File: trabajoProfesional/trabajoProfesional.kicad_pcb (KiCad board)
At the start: 2 copper layers, 21 parts, among them J1 SYSOUT, J2 BATPositve, J3 BATNegative, J4 GPIO5, J5 GPIO4, J6 GPIO3, J7 GPIO2, J8 GPIO1, U1 TS51224-M000WCSR

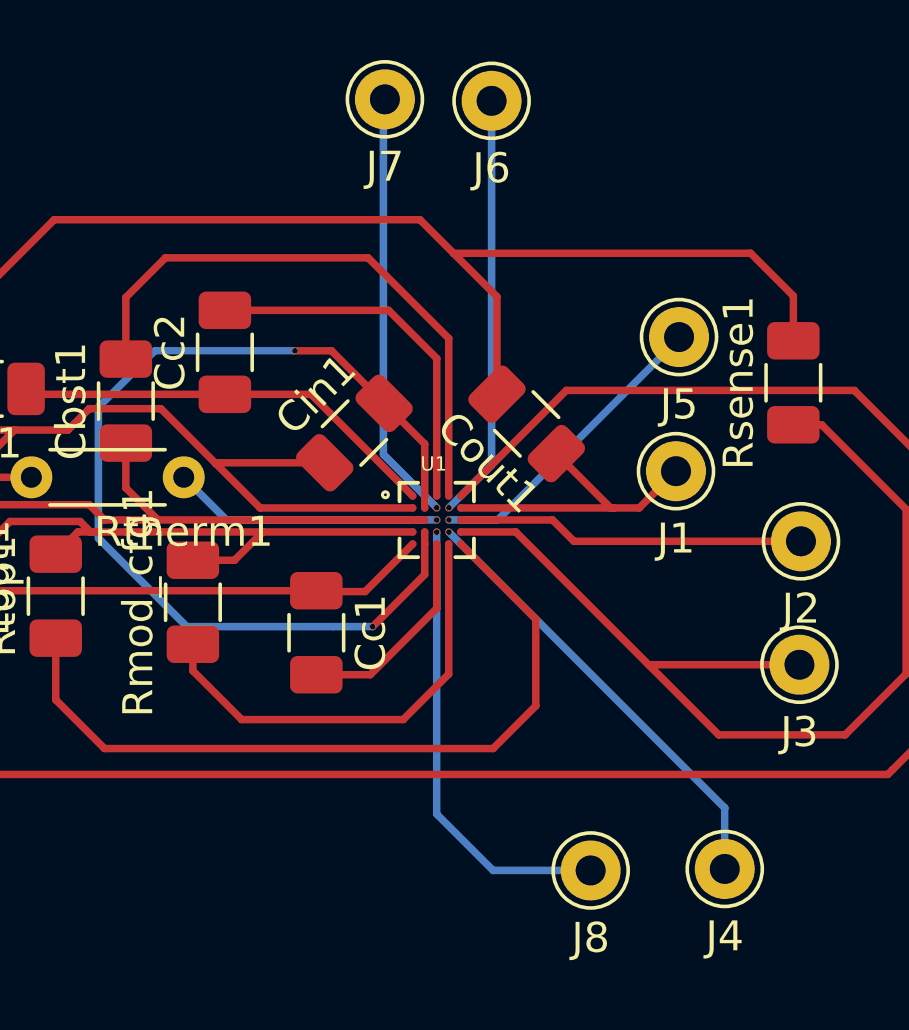
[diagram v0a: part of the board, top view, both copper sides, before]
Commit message: ahora se modifico la via para que quede lo mas grande posible y fuera del pin VGA
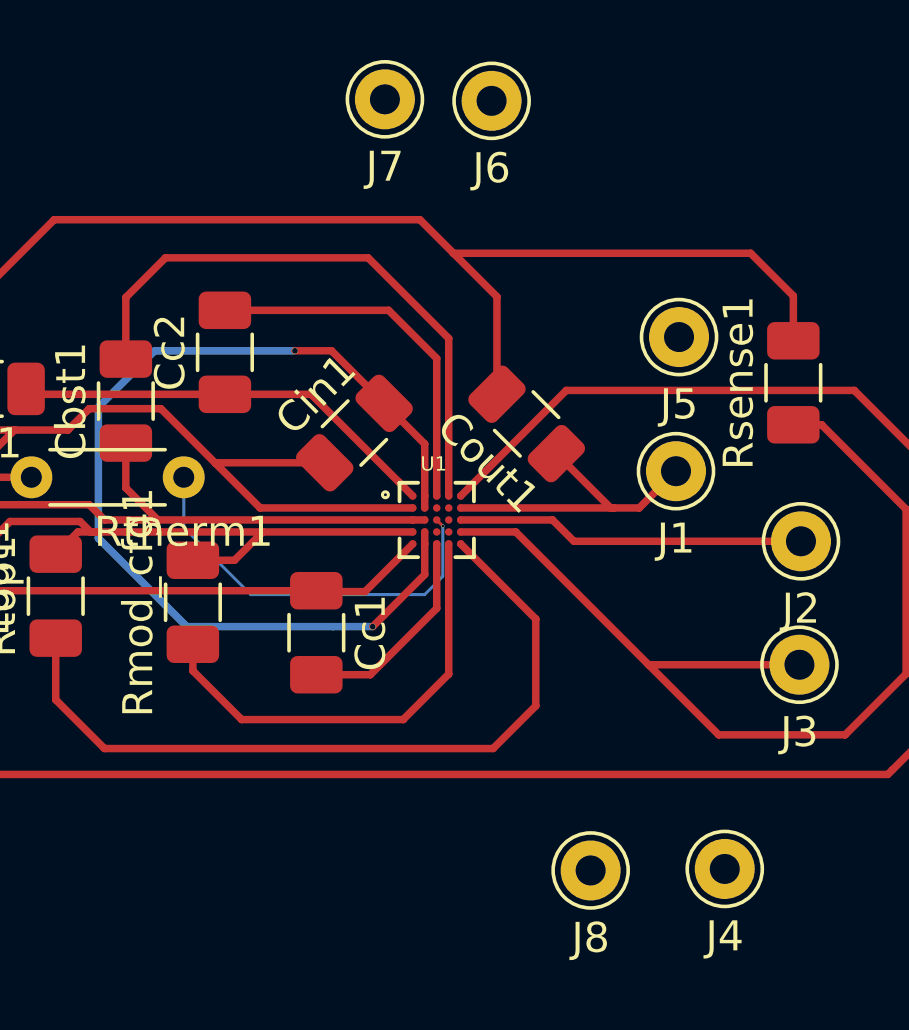
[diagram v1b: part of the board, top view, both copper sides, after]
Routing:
- net Net-(J8-Pad1): track 15.3 -> 0.00 mm, vias 1 -> 0
- net Net-(J4-Pad1): track 15.0 -> 0.00 mm, vias 1 -> 0
- net Net-(J7-Pad1): track 14.4 -> 0.00 mm, vias 1 -> 0
- net Net-(J6-Pad1): track 14.2 -> 0.00 mm, vias 1 -> 0
- net Net-(J5-Pad1): track 10.2 -> 0.00 mm, vias 1 -> 0
- net Net-(Rtherm1-Pad1): track 9.02 -> 13.5 mm

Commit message: va el parche con el ultimo mod del los pines anulados
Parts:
- removed J4: GPIO5, Connector_Pin:Pin_D1.0mm_L10.0mm
- removed J5: GPIO4, Connector_Pin:Pin_D1.0mm_L10.0mm
- removed J6: GPIO3, Connector_Pin:Pin_D1.0mm_L10.0mm
- removed J7: GPIO2, Connector_Pin:Pin_D1.0mm_L10.0mm
- removed J8: GPIO1, Connector_Pin:Pin_D1.0mm_L10.0mm
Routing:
- net Net-(Cin1-Pad2): track 33.7 -> 21.2 mm
- net Net-(Rtherm1-Pad1): track 13.5 -> 18.6 mm
- net Net-(Rmod_cfg1-Pad1): track 15.1 -> 15.7 mm
- net Net-(Cc1-Pad2): track 7.08 -> 6.47 mm
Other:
- net class Default: clearance 0.02 -> 0.0002
- rule trace_clearance: 0.02 -> 0.0002
- rule trace_min: 0.002 -> 0.0002
- rule via_min_drill: 0.0003 -> 0.00003
- rule via_min_size: 0.0004 -> 0.00004

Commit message: se agregan todos los componentes al squematico
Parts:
- removed Cbst1, Cc1, Cc2, Cin1, Cout1, Cs1: C, Capacitor_SMD:C_1206_3216Metric
- removed J1: SYSOUT, Connector_Pin:Pin_D1.0mm_L10.0mm
- removed J2: BATPositve, Connector_Pin:Pin_D1.0mm_L10.0mm
- removed J3: BATNegative, Connector_Pin:Pin_D1.0mm_L10.0mm
- removed Lin1: L, Inductor_SMD:L_Neosid_Air-Coil_SML_6-10turn_HAM0631A-HAM1031A
- removed Lout1: L, Inductor_SMD:L_1206_3216Metric
- removed Rmod_cfg1, Rsense1, Rtop1: R, Resistor_SMD:R_1206_3216Metric
- removed Rtherm1: R, Resistor_THT:R_Axial_DIN0204_L3.6mm_D1.6mm_P5.08mm_Horizontal
- removed U1: TS51224-M000WCSR, TS51224-M000WCSR:BGA25N40P5X5_230X230X57N
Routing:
- net GND: track 95.2 -> 0.00 mm
- net Net-(Lout1-Pad2): track 65.1 -> 0.00 mm
- net Net-(J3-Pad1): track 33.9 -> 0.00 mm
- net Net-(Cc1-Pad1): track 28.0 -> 0.00 mm
- net Net-(Rtop1-Pad1): track 25.8 -> 0.00 mm
- net Net-(Cin1-Pad2): track 21.2 -> 0.00 mm, vias 2 -> 0
- net Net-(Cbst1-Pad1): track 19.8 -> 0.00 mm
- net Net-(Cbst1-Pad2): track 19.7 -> 0.00 mm
- net Net-(Rtherm1-Pad1): track 18.6 -> 0.00 mm, vias 1 -> 0
- net Net-(Rmod_cfg1-Pad1): track 15.7 -> 0.00 mm
- net Net-(Cc2-Pad1): track 14.4 -> 0.00 mm
- net Net-(Cc2-Pad2): track 12.3 -> 0.00 mm
- net Net-(J2-Pad1): track 11.6 -> 0.00 mm
- net Net-(Cout1-Pad1): track 10.3 -> 0.00 mm
- net Net-(Cs1-Pad2): track 7.86 -> 0.00 mm
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
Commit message: empezando el pcb
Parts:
- added AdministracionBateria1: SC810ULTRT, SC810:SON50P200X200X60-7N-D, F.Cu at (77.8, 76.9)
- added C1: 10n, Capacitor_SMD:C_2816_7142Metric, F.Cu at (211.4, 86.5)
- added C2: 10n, Capacitor_SMD:C_2816_7142Metric, F.Cu at (173.1, 90.9)
- added C3: 10n, Capacitor_SMD:C_2816_7142Metric, F.Cu at (218.4, 86.5)
- added C4: 10n, Capacitor_SMD:C_2816_7142Metric, F.Cu at (214.7, 101.5)
- added C5: 10n, Capacitor_SMD:C_2816_7142Metric, F.Cu at (202.5, 90.7)
- added C6: 100n, Capacitor_SMD:C_2816_7142Metric, F.Cu at (143.6, 142.1)
- added Cbat1: 2.2u, Capacitor_SMD:C_Elec_3x5.4, F.Cu at (82.3, 86.6)
- added Cbst1: 47n, Capacitor_SMD:C_2816_7142Metric, F.Cu at (80.9, 61.7)
- added Cc1: 1n, Capacitor_SMD:CP_Elec_3x5.3, F.Cu at (56.4, 75.5)
- added Cc2: 1n, Capacitor_SMD:CP_Elec_3x5.3, F.Cu at (68.6, 61.6)
- added Cin1: 22u, Capacitor_SMD:CP_Elec_3x5.3, F.Cu at (62.9, 90.7)
- added Cin2: 100n, Capacitor_SMD:CP_Elec_3x5.3, F.Cu at (89.9, 105.0)
- added Cout1: 22u, Capacitor_SMD:CP_Elec_3x5.3, F.Cu at (101.1, 112.1)
- added Cout2: 22u, Capacitor_SMD:CP_Elec_3x5.3, F.Cu at (81.7, 93.0)
- added Cout3: 22u, Capacitor_SMD:CP_Elec_3x5.3, F.Cu at (96.3, 74.4)
- added Cout4: 22u, Capacitor_SMD:CP_Elec_3x5.3, F.Cu at (101.2, 95.0)
- added Cs2: 10n, Capacitor_SMD:CP_Elec_3x5.3, F.Cu at (60.8, 67.5)
- added Cvin1: 2.2u, Capacitor_SMD:C_Elec_3x5.4, F.Cu at (101.0, 106.5)
- added D1: 1.8, Diode_SMD:D_SC-80, F.Cu at (190.1, 106.5)
- added D2: 1.8, Diode_SMD:D_SC-80, F.Cu at (184.9, 106.6)
- added D3: 1.8, Diode_SMD:D_SC-80, F.Cu at (182.2, 106.7)
- added D4: 1.8, Diode_SMD:D_SC-80, F.Cu at (187.5, 106.6)
- added DbyPass1: D_Schottky, Diode_SMD:D_SOD-323F, F.Cu at (88.6, 76.6)
- added DriverPotencia1: HV7360GA-G, HV7360:HV7360GAG, F.Cu at (186.4, 90.4)
- added Lout1: 4.7u, Inductor_SMD:L_7.3x7.3_H3.5, F.Cu at (95.0, 62.0)
- added PiezoElectrico1: UTR-1440K-TT-R, Connector_PinHeader_2.54mm:PinHeader_1x02_P2.54mm_Vertical, F.Cu at (189.9, 114.1)
- added R1: 10k, Resistor_SMD:R_1206_3216Metric, F.Cu at (129.0, 144.5)
- added R1fb1: 46k, Resistor_SMD:R_1206_3216Metric, F.Cu at (90.0, 92.3)
- added R2: 10k, Resistor_SMD:R_1206_3216Metric, F.Cu at (111.7, 137.0)
- added R2fb1: 10k, Resistor_SMD:R_1206_3216Metric, F.Cu at (56.3, 84.8)
- added RIPRGM1: R, Resistor_SMD:R_1206_3216Metric, F.Cu at (75.6, 85.5)
- added RecpetorPotenciaInalambrica1: TS51223-M000WCSR, TS51223:BGA20C40P4X5_190X230X58, F.Cu at (73.8, 69.2)
- added Riso_pd1: R, Resistor_SMD:R_1206_3216Metric, F.Cu at (101.0, 101.2)
- added Rmod_cfg1: 60k, Resistor_SMD:R_1206_3216Metric, F.Cu at (69.4, 91.3)
- added Rstatus1: R, Resistor_SMD:R_1206_3216Metric, F.Cu at (82.7, 81.8)
- added SensorPresion1: MS583730BA01-50, Connector_PinSocket_2.54mm:PinSocket_2x02_P2.54mm_Vertical_SMD, F.Cu at (126.9, 137.4)
- added T1: MPMOS, Package_TO_SOT_SMD:TSOT-23, F.Cu at (88.7, 83.4)
- added TrinketM0: micro, Connector_PinHeader_1.00mm:PinHeader_2x05_P1.00mm_Vertical, F.Cu at (135.3, 50.4)
- added coil1: L, Connector_PinHeader_2.54mm:PinHeader_1x02_P2.54mm_Vertical, F.Cu at (46.8, 67.6)
- added opt1: D_Schottky, Diode_SMD:D_SOD-323F, F.Cu at (85.5, 78.1)

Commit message: paso previo PCB
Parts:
- removed TrinketM0: micro, Connector_PinHeader_1.00mm:PinHeader_2x05_P1.00mm_Vertical
- removed coil1: L, Connector_PinHeader_2.54mm:PinHeader_1x02_P2.54mm_Vertical
- added 10V1: Conn_01x01_Male, Connector_PinHeader_1.00mm:PinHeader_1x01_P1.00mm_Vertical, F.Cu at (194.6, 97.7)
- added BatPositivo1: Conn_01x01_Male, Connector_PinHeader_1.00mm:PinHeader_1x01_P1.00mm_Vertical, F.Cu at (68.4, 109.1)
- added Coil1: Conn_01x01_Male, Connector_PinHeader_1.00mm:PinHeader_1x01_P1.00mm_Vertical, F.Cu at (60.8, 64.8)
- added Coil2: Conn_01x01_Male, Connector_PinHeader_1.00mm:PinHeader_1x01_P1.00mm_Vertical, F.Cu at (65.6, 72.9)
- added HV+1: Conn_01x01_Male, Connector_PinSocket_2.54mm:PinSocket_1x01_P2.54mm_Vertical, F.Cu at (198.9, 76.2)
- added HV-1: Conn_01x01_Male, Connector_PinSocket_2.54mm:PinSocket_1x01_P2.54mm_Vertical, F.Cu at (207.7, 114.2)
- added U1: 1501, Connector_PinHeader_1.00mm:PinHeader_2x05_P1.00mm_Vertical, F.Cu at (125.3, 103.6)
- added batGND1: Conn_01x01_Male, Connector_PinHeader_1.00mm:PinHeader_1x01_P1.00mm_Vertical, F.Cu at (76.7, 113.7)
- moved AdministracionBateria1 25.6 mm to (101.8, 67.8), turned to 90 degrees
- moved Cc1 15.4 mm to (71.8, 73.7)
- moved Cin1 13.2 mm to (70.2, 79.8)
- moved Lout1 9.31 mm to (88.5, 68.8)
- moved Cout3 7.11 mm to (96.6, 67.3), turned to 270 degrees
- moved Cs2 5.57 mm to (65.6, 64.7)
- moved Cbst1 4.69 mm to (81.4, 66.3), turned to 90 degrees
- moved Cc2 4.63 mm to (72.0, 64.7)
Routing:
- net Net-(Cbst1-Pad1): track 0.00 -> 11.9 mm
- net Net-(Cc1-Pad2): track 0.00 -> 10.8 mm
- net Net-(Cin1-Pad2): track 0.00 -> 10.5 mm
- net Net-(AdministracionBateria1-Pad1): track 0.00 -> 9.58 mm
- net Net-(Cbst1-Pad2): track 0.00 -> 9.03 mm
- net Net-(Cc2-Pad1): track 0.00 -> 8.19 mm
- net Net-(Cc1-Pad1): track 0.00 -> 4.02 mm
- net Net-(Cc2-Pad2): track 0.00 -> 3.88 mm
- net Net-(Coil1-Pad1): track 0.00 -> 3.32 mm
- net Net-(R1fb1-Pad2): track 0.00 -> 0.92 mm
- net Net-(RecpetorPotenciaInalambrica1-PadD4): track 0.00 -> 0.86 mm
- net GND: track 0.00 -> 0.80 mm

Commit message: PCB falta una conexion
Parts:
- 10V1, BatPositivo1, Coil1, Coil2, batGND1: footprint Connector_PinHeader_1.00mm:PinHeader_1x01_P1.00mm_Vertical -> TestPoint:TestPoint_Pad_D2.5mm
- HV+1, HV-1: footprint Connector_PinSocket_2.54mm:PinSocket_1x01_P2.54mm_Vertical -> TestPoint:TestPoint_Pad_D2.5mm
- PiezoElectrico1: footprint Connector_PinHeader_2.54mm:PinHeader_1x02_P2.54mm_Vertical -> Connector_PinHeader_2.54mm:PinHeader_1x02_P2.54mm_Vertical_SMD_Pin1Left
- moved C1 89.5 mm to (121.9, 88.3)
- moved C3 89.5 mm to (129.0, 88.4)
- moved C4 87.4 mm to (135.1, 65.3), turned to 270 degrees
- moved HV-1 82.5 mm to (136.4, 72.7)
- moved C5 78.9 mm to (127.0, 67.7), turned to 0 degrees
- moved 10V1 73.8 mm to (122.8, 80.8)
- moved HV+1 67.8 mm to (131.2, 73.8)
- moved BatPositivo1 63.9 mm to (112.6, 62.9)
- moved PiezoElectrico1 63.8 mm to (143.7, 70.1), turned to 0 degrees
- moved batGND1 61.2 mm to (109.0, 61.7)
- moved C6 60.4 mm to (115.2, 88.8)
- moved D1 57.6 mm to (140.8, 76.6), turned to 0 degrees
- moved R1 56.3 mm to (107.5, 92.5)
- moved SensorPresion1 54.9 mm to (106.2, 86.6)
- moved DriverPotencia1 54.5 mm to (133.0, 79.5), turned to 90 degrees
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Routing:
- net Net-(AdministracionBateria1-Pad1): track 9.58 -> 73.8 mm
- net /Salida/Alimentacion: track 0.00 -> 51.9 mm
- net Net-(C6-Pad2): track 0.00 -> 47.3 mm
- net /Bateria/Cargando: track 0.00 -> 36.8 mm
- net 10V: track 0.00 -> 27.9 mm
- net +Bat: track 0.00 -> 27.5 mm
- net /Salida/SP1ONOFF: track 0.00 -> 23.5 mm
- net /Salida/SN1ONOFF: track 0.00 -> 21.5 mm
- net +HV: track 0.00 -> 20.1 mm
- net SDAPresion: track 0.00 -> 17.0 mm
- net SCLPresion: track 0.00 -> 15.6 mm
- net -HV: track 0.00 -> 14.6 mm
- net Net-(R1fb1-Pad2): track 0.92 -> 15.3 mm
- net Net-(D1-Pad2): track 0.00 -> 10.6 mm
- net Net-(C6-Pad1): track 0.00 -> 6.88 mm
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- added copper zone on F.Cu, net GND

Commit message: va el circuito
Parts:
- removed AdministracionBateria1: SC810ULTRT, SC810:SON50P200X200X60-7N-D
- removed Coil1: Conn_01x01_Male, TestPoint:TestPoint_Pad_D2.5mm
- removed Rstatus1: R, Resistor_SMD:R_1206_3216Metric
- added BatAd: SC810ULTRT, SC810:SON50P200X200X60-7N-D, F.Cu at (102.3, 68.7)
- added Coil+: Conn_01x01_Male, TestPoint:TestPoint_Pad_D2.5mm, F.Cu at (60.8, 64.8)
- added Rstat: R, Resistor_SMD:R_1806_4516Metric, F.Cu at (90.2, 68.1)
- C1, C2, C3, C4, C5, C6: footprint Capacitor_SMD:C_2816_7142Metric -> Capacitor_SMD:C_0201_0603Metric
- Cbst: renamed from Cbst1; footprint Capacitor_SMD:C_2816_7142Metric -> Capacitor_SMD:C_0201_0603Metric
- R1, R2, RIPRGM1: footprint Resistor_SMD:R_1206_3216Metric -> Resistor_SMD:R_0201_0603Metric
- R1fb: renamed from R1fb1; footprint Resistor_SMD:R_1206_3216Metric -> Resistor_SMD:R_0201_0603Metric
- R2fb: renamed from R2fb1; footprint Resistor_SMD:R_1206_3216Metric -> Resistor_SMD:R_0201_0603Metric
- Rcfg: renamed from Rmod_cfg1; footprint Resistor_SMD:R_1206_3216Metric -> Resistor_SMD:R_0201_0603Metric
- Riso: renamed from Riso_pd1; footprint Resistor_SMD:R_1206_3216Metric -> Resistor_SMD:R_0201_0603Metric
- SP: renamed from SensorPresion1; footprint Connector_PinSocket_2.54mm:PinSocket_2x02_P2.54mm_Vertical_SMD -> Connector_PinHeader_2.54mm:PinHeader_2x02_P2.54mm_Vertical
- moved C3 23.4 mm to (106.7, 81.4), turned to 180 degrees
- moved Piezo 22.6 mm to (121.2, 70.7)
- moved HV-1 21.2 mm to (115.4, 70.2)
- moved HV+1 20.8 mm to (110.7, 70.4)
- moved C4 18.6 mm to (118.1, 72.8), turned to 180 degrees
- moved D4 18.3 mm to (122.6, 79.8)
- moved D1 18.3 mm to (122.5, 75.3)
- moved D2 18.3 mm to (122.5, 76.9)
- moved D3 18.3 mm to (122.6, 78.4)
- moved Driver 18.3 mm to (114.8, 78.2)
- moved C5 16.9 mm to (111.3, 73.9)
- moved 10V1 16.3 mm to (106.6, 78.8)
- moved C6 15.4 mm to (101.6, 81.4), turned to 90 degrees
- moved C2 15.3 mm to (108.1, 73.5), turned to 90 degrees
- moved C1 14.5 mm to (109.2, 81.4), turned to 0 degrees
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- renumbered BatPositivo1 to Bat+, batGND1 to Bat-, Cbat1 to Cbat, Cout1 to Co1, Cout4 to Co4, Coil2 to Coil-, DbyPass1 to Dbp, DriverPotencia1 to Driver, Lout1 to Lo, U1 to M0, PiezoElectrico1 to Piezo, T1 to T, RecpetorPotenciaInalambrica1 to WPR
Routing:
- net Net-(C6-Pad2): track 47.3 -> 20.9 mm
- net /Salida/Alimentacion: track 51.9 -> 26.4 mm
- net /Bateria/Cargando: track 36.8 -> 19.0 mm
- net Net-(AdministracionBateria1-Pad1): track 73.8 -> 58.4 mm
- net 10V: track 27.9 -> 13.1 mm
- net SDAPresion: track 17.0 -> 8.70 mm
- net +HV: track 20.1 -> 13.0 mm
- net /Salida/SN1ONOFF: track 21.5 -> 14.9 mm
- net /Salida/SP1ONOFF: track 23.5 -> 17.0 mm
- net Net-(R1fb1-Pad2): track 15.3 -> 9.23 mm
- net +Bat: track 27.5 -> 22.0 mm
- net -HV: track 14.6 -> 10.0 mm
- net GND: track 7.33 -> 3.13 mm
- net Net-(C6-Pad1): track 6.88 -> 3.28 mm
- net Net-(RecpetorPotenciaInalambrica1-PadD4): track 6.21 -> 3.37 mm
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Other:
- board outline added: 66.2 x 25.4 mm
